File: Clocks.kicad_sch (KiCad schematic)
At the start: 87 parts, among them U1 MC100LVEL16, U13 MC100EL14, U14 1821-4731, U15 SY89421V, U16 LM311, U73 MC100LVEL16, U74 MC10EL34, U79 OSC_HS-2810

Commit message: Add component values, some more nets
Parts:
- C177, C178, C179, C182, C184, C185, C186: value ? -> 0.047uF
- C180, C202, C203, C204, C205, C206, C207, C208, C209, C210, C211, C212, C213, C214, C215: value ? -> 3.3nF
- C181: value ? -> 3.9nF
- C183, C187, C188, C189, C190: value ? -> 1nF
- C461: value ? -> 360pF
- R221, R222: value ? -> 56.2
- R223: value ? -> 38.3
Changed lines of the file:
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@@
 			)
 		)
-		(property "Value" "?"
+		(property "Value" "3.3nF"
 			(at 363.22 62.2362 0)
 			(effects
@@
 			)
 		)
-		(property "Value" "?"
+		(property "Value" "3.3nF"
 			(at 287.02 58.4262 0)
 			(effects
@@
 			)
 		)
-		(property "Value" "?"
+		(property "Value" "1nF"
 			(at 26.67 170.1862 0)
 			(effects
@@
 			)
 		)
-		(property "Value" "?"
+		(property "Value" "3.3nF"
 			(at 287.02 78.7462 0)
 			(effects
@@
 			)
 		)
-		(property "Value" "?"
+		(property "Value" "3.3nF"
 			(at 278.13 78.7462 0)
 			(effects
@@
 			)
 		)
-		(property "Value" "?"
+		(property "Value" "56.2"
 			(at 397.256 182.118 0)
 			(effects
@@
 			)
 		)
-		(property "Value" "?"
+		(property "Value" "0.047uF"
 			(at 163.83 179.0762 0)
 			(effects
@@
 			)
 		)
-		(property "Value" "?"
+		(property "Value" "1nF"
 			(at 229.108 139.192 90)
 			(effects
@@
 			)
 		)
-		(property "Value" "?"
+		(property "Value" "3.3nF"
 			(at 321.31 116.8462 0)
 			(effects
@@
 			)
 		)
-		(property "Value" "?"
+		(property "Value" "3.3nF"
 			(at 295.91 78.7462 0)
 			(effects
@@
 			)
 		)
-		(property "Value" "?"
+		(property "Value" "3.3nF"
 			(at 354.33 62.2362 0)
 			(effects
@@
 			)
 		)
-		(property "Value" "?"
+		(property "Value" "0.047uF"
 			(at 124.46 187.9662 0)
 			(effects
@@
 			)
 		)
-		(property "Value" "?"
+		(property "Value" "3.3nF"
 			(at 304.8 78.7462 0)
 			(effects
@@
 			)
 		)
-		(property "Value" "?"
+		(property "Value" "3.3nF"
 			(at 229.87 85.0962 0)
 			(effects
@@
 			)
 		)
-		(property "Value" "?"
+		(property "Value" "3.9nF"
 			(at 240.03 85.0962 0)
 			(effects
@@
 			)
 		)
-		(property "Value" "?"
+		(property "Value" "0.047uF"
 			(at 162.56 90.1762 0)
 			(effects
@@
 			)
 		)
-		(property "Value" "?"
+		(property "Value" "38.3"
 			(at 386.588 192.024 0)
 			(effects
@@
 			)
 		)
-		(property "Value" "?"
+		(property "Value" "3.3nF"
 			(at 313.69 58.4262 0)
 			(effects
@@
 			)
 		)
-		(property "Value" "?"
+		(property "Value" "3.3nF"
 			(at 313.69 78.7462 0)
 			(effects
@@
 			)
 		)
-		(property "Value" "?"
+		(property "Value" "0.047uF"
 			(at 69.342 153.416 90)
 			(effects
@@
 			)
 		)
-		(property "Value" "?"
+		(property "Value" "3.3nF"
 			(at 295.91 58.4262 0)
 			(effects
@@
 			)
 		)
-		(property "Value" "?"
+		(property "Value" "3.3nF"
 			(at 312.42 116.8462 0)
 			(effects
@@
 			)
 		)
-		(property "Value" "?"
+		(property "Value" "3.3nF"
 			(at 278.13 58.4262 0)
 			(effects
@@
 			)
 		)
-		(property "Value" "?"
+		(property "Value" "1nF"
 			(at 415.29 194.3162 0)
 			(effects
@@
 			)
 		)
-		(property "Value" "?"
+		(property "Value" "1nF"
 			(at 405.13 194.3162 0)
 			(effects
@@
 			)
 		)
-		(property "Value" "?"
+		(property "Value" "360pF"
 			(at 436.626 193.04 0)
 			(effects
@@
 			)
 		)
-		(property "Value" "?"
+		(property "Value" "3.3nF"
 			(at 304.8 58.4262 0)
 			(effects
@@
 			)
 		)
-		(property "Value" "?"
+		(property "Value" "0.047uF"
 			(at 214.63 85.0962 0)
 			(effects
@@
 			)
 		)
-		(property "Value" "?"
+		(property "Value" "56.2"
 			(at 384.048 181.864 0)
 			(effects
@@
 			)
 		)
-		(property "Value" "?"
+		(property "Value" "0.047uF"
 			(at 73.914 166.624 90)
 			(effects
@@
 			)
 		)
-		(property "Value" "?"
+		(property "Value" "1nF"
 			(at 134.62 187.9662 0)
 			(effects
@@
 			)
 		)
-		(property "Value" "?"
+		(property "Value" "0.047uF"
 			(at 104.14 90.1762 0)
 			(effects

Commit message: complete outer layers
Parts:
- RN1, RN2, RN3, RN4, RN5, RN6, RN7, RN8: footprint Resistor_SMD:R_Array_Convex_4x0603 -> hp16717:HP_R_Array_Convex_4x0603
- U13, U15: footprint Package_SO:SOIC-20W_7.5x12.8mm_P1.27mm -> hp16717:HP_SOIC-20W_7.5x12.8mm_P1.27mm
- U79: footprint Oscillator:Oscillator_DIP-14 -> hp16717:HP_Oscillator_DIP-14
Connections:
- net +3V3: no longer C211.1
- net -1V7: now also C211.1
- net 100M_SYSCLK2 renamed 100M_SYSCLK2_P
- net TZCLK1 renamed TZCLK1_P
- net TZCLK2 renamed TZCLK2_P
- net TZCLK3 renamed TZCLK3_P
- net TZCLK4 renamed TZCLK4_P
- net TZCLK5 renamed TZCLK5_P
- net TZCLKI renamed TZCLKI_P
- net TZCLKO1 renamed TZCLKO1_P
- net TZCLKO10 renamed TZCLKO10_P
- net TZCLKO2 renamed TZCLKO2_P
- net TZCLKO3 renamed TZCLKO3_P
- net TZCLKO4 renamed TZCLKO4_P
- net TZCLKO5 renamed TZCLKO5_P
- net TZCLKO6 renamed TZCLKO6_P
- net TZCLKO7 renamed TZCLKO7_P
- net TZCLKO8 renamed TZCLKO8_P
- net TZCLKO9 renamed TZCLKO9_P
- net ~{100M_SYSCLK2} renamed 100M_SYSCLK2_N
- net ~{TZCLK1} renamed TZCLK1_N
- net ~{TZCLK2} renamed TZCLK2_N
- net ~{TZCLK3} renamed TZCLK3_N
- net ~{TZCLK4} renamed TZCLK4_N
- net ~{TZCLK5} renamed TZCLK5_N
- net ~{TZCLKI} renamed TZCLKI_N
- net ~{TZCLKO10} renamed TZCLKO10_N
- net ~{TZCLKO1} renamed TZCLKO1_N
- net ~{TZCLKO2} renamed TZCLKO2_N
- net ~{TZCLKO3} renamed TZCLKO3_N
- net ~{TZCLKO4} renamed TZCLKO4_N
- net ~{TZCLKO5} renamed TZCLKO5_N
- net ~{TZCLKO6} renamed TZCLKO6_N
- net ~{TZCLKO7} renamed TZCLKO7_N
- net ~{TZCLKO8} renamed TZCLKO8_N
- net ~{TZCLKO9} renamed TZCLKO9_N
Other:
- moved on the sheet: C211

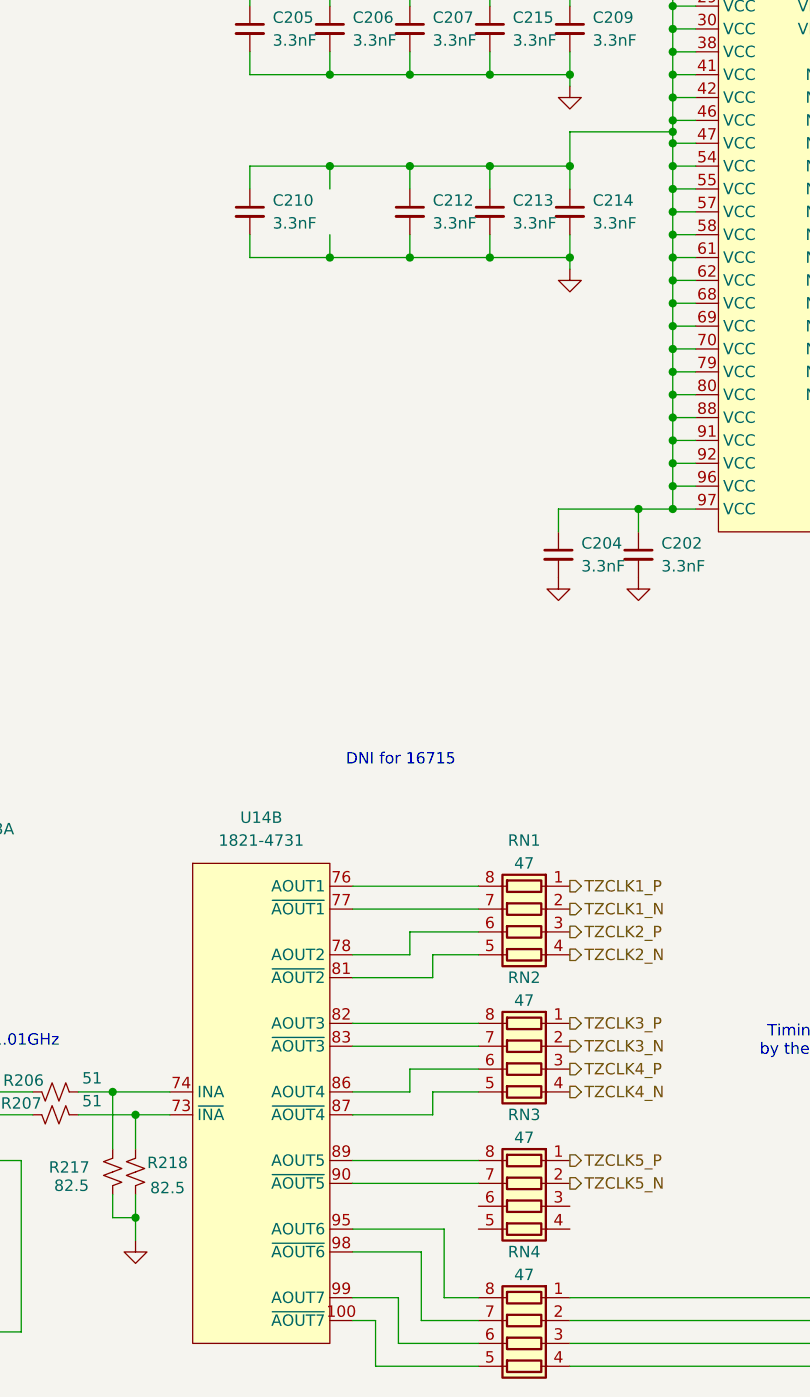
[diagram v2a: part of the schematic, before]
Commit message: schematic cleanup, arrange silk designators
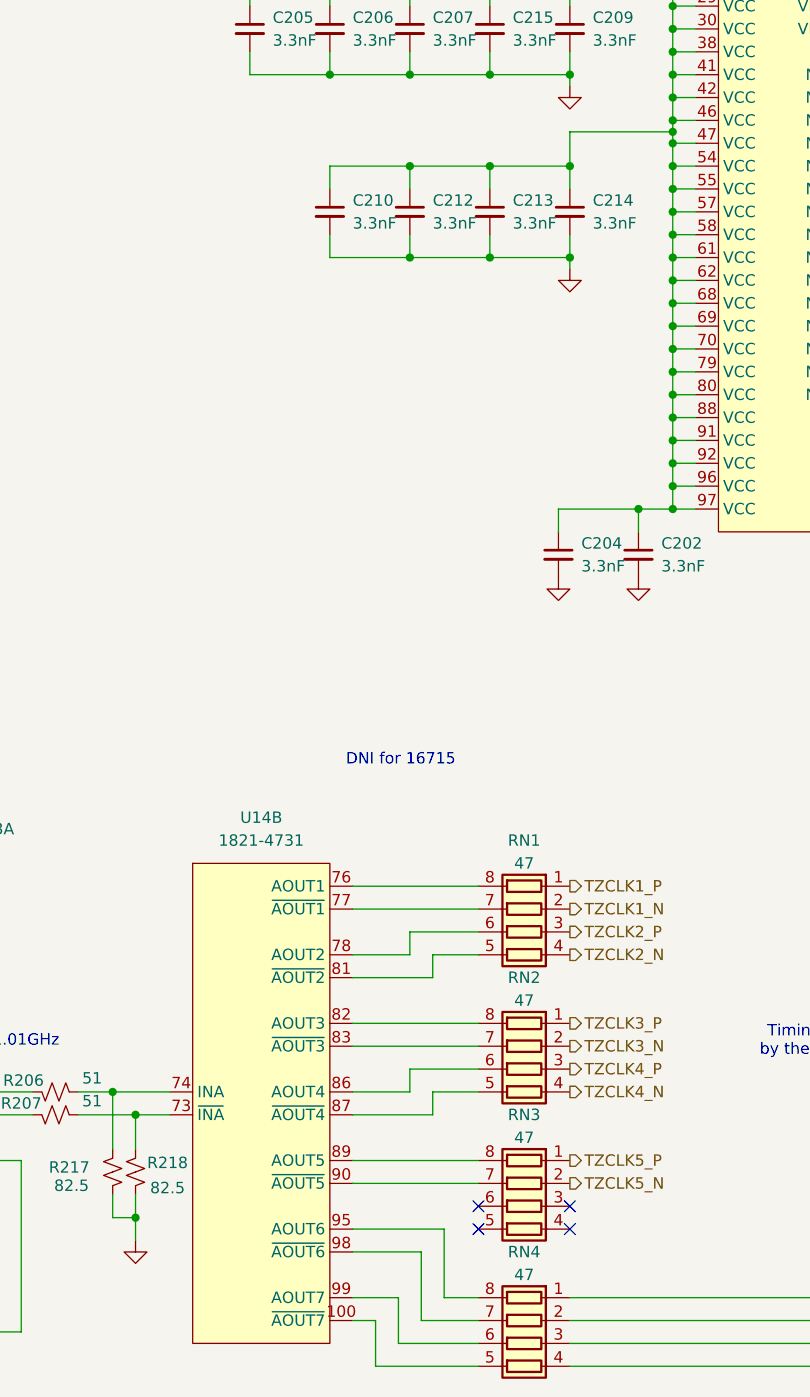
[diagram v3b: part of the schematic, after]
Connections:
- no-connect marks 10 -> 14
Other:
- moved on the sheet: C210
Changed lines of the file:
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@@
 	)
 	(junction
-		(at 284.48 72.39)
-		(diameter 0)
-		(color 0 0 0 0)
-	)
-	(junction
 		(at 311.15 72.39)
 		(diameter 0)
@@
 	)
 	(junction
-		(at 284.48 82.55)
-		(diameter 0)
-		(color 0 0 0 0)
-	)
-	(junction
 		(at 425.45 24.13)
 		(diameter 0)
@@
 	)
 	(no_connect
+		(at 311.15 190.5)
+	)
+	(no_connect
 		(at 420.37 76.2)
 	)
 	(no_connect
+		(at 300.99 187.96)
+	)
+	(no_connect
+		(at 300.99 190.5)
+	)
+	(no_connect
 		(at 435.61 177.8)
 	)
@@
 	)
 	(no_connect
+		(at 311.15 187.96)
+	)
+	(no_connect
 		(at 96.52 53.34)
 	)
@@
 	(wire
 		(pts
-			(xy 284.48 72.39) (xy 293.37 72.39)
-		)
-		(stroke
-			(width 0)
-			(type default)
-		)
-	)
-	(wire
-		(pts
 			(xy 53.34 45.72) (xy 55.88 45.72)
 		)
@@
 	(wire
 		(pts
-			(xy 284.48 82.55) (xy 284.48 80.01)
-		)
-		(stroke
-			(width 0)
-			(type default)
-		)
-	)
-	(wire
-		(pts
 			(xy 438.15 91.44) (xy 438.15 146.05)
 		)
@@
 	(wire
 		(pts
-			(xy 275.59 82.55) (xy 284.48 82.55)
+			(xy 284.48 82.55) (xy 293.37 82.55)
 		)
 		(stroke
@@
 	(wire
 		(pts
-			(xy 284.48 72.39) (xy 284.48 74.93)
-		)
-		(stroke
-			(width 0)
-			(type default)
-		)
-	)
-	(wire
-		(pts
 			(xy 420.37 57.15) (xy 443.23 57.15)
 		)
@@
 	(wire
 		(pts
-			(xy 275.59 72.39) (xy 275.59 74.93)
+			(xy 284.48 72.39) (xy 284.48 74.93)
 		)
 		(stroke
@@
 	(wire
 		(pts
-			(xy 275.59 82.55) (xy 275.59 80.01)
+			(xy 284.48 82.55) (xy 284.48 80.01)
 		)
 		(stroke
@@
 	(wire
 		(pts
-			(xy 284.48 82.55) (xy 293.37 82.55)
-		)
-		(stroke
-			(width 0)
-			(type default)
-		)
-	)
-	(wire
-		(pts
 			(xy 205.74 190.5) (xy 205.74 185.42)
 		)
@@
 	(wire
 		(pts
-			(xy 275.59 72.39) (xy 284.48 72.39)
+			(xy 284.48 72.39) (xy 293.37 72.39)
 		)
 		(stroke
@@
 	(symbol
 		(lib_id "Device:C_Small")
-		(at 275.59 77.47 0)
+		(at 284.48 77.47 0)
 		(unit 1)
 		(exclude_from_sim no)
@@
 		(dnp no)
 		(property "Reference" "C210"
-			(at 278.13 76.2062 0)
+			(at 287.02 76.2062 0)
 			(effects
 				(font
@@
 		)
 		(property "Value" "3.3nF"
-			(at 278.13 78.7462 0)
+			(at 287.02 78.7462 0)
 			(effects
 				(font
@@
 		)
 		(property "Footprint" "hp16717:HP_0603"
-			(at 275.59 77.47 0)
+			(at 284.48 77.47 0)
 			(effects
 				(font
@@
 		)
 		(property "Datasheet" "~"
-			(at 275.59 77.47 0)
+			(at 284.48 77.47 0)
 			(effects
 				(font
@@
 		)
 		(property "Description" "Unpolarized capacitor, small symbol"
-			(at 275.59 77.47 0)
+			(at 284.48 77.47 0)
 			(effects
 				(font

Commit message: add test points
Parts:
- added TP1069, TP1070, TP1072, TP1073, TP670, TP671, TP672, TP673, TP674, TP675, TP676, TP808, TP809, TP810, TP811, TP812, TP813, TP816, TP817, TP818, TP823, TP824: ?, hp16717:HP_TP30, symbol Connector:TestPoint_Alt
- added TP1071: +3V3, hp16717:HP_TP30, symbol Connector:TestPoint_Alt
- added TP661, TP807: HPCLK_D0, hp16717:HP_TP30, symbol Connector:TestPoint_Alt
- added TP662, TP806: HPCLK_D1, hp16717:HP_TP30, symbol Connector:TestPoint_Alt
- added TP663, TP804: HPCLK_D3, hp16717:HP_TP30, symbol Connector:TestPoint_Alt
- added TP664, TP805: HPCLK_D2, hp16717:HP_TP30, symbol Connector:TestPoint_Alt
- added TP665, TP800: HPCLK_D7, hp16717:HP_TP30, symbol Connector:TestPoint_Alt
- added TP666, TP801: HPCLK_D6, hp16717:HP_TP30, symbol Connector:TestPoint_Alt
- added TP667, TP802: HPCLK_D5, hp16717:HP_TP30, symbol Connector:TestPoint_Alt
- added TP668, TP803: HPCLK_D4, hp16717:HP_TP30, symbol Connector:TestPoint_Alt
- added TP669, TP677: 3V3, hp16717:HP_TP30, symbol Connector:TestPoint_Alt
- added TP814: +5V, hp16717:HP_TP30, symbol Connector:TestPoint_Alt
- added TP815, TP825, TP826: GND, hp16717:HP_TP30, symbol Connector:TestPoint_Alt
- added TP819: VBB, hp16717:HP_TP30, symbol Connector:TestPoint_Alt
- added TP820: FOUT, hp16717:HP_TP30, symbol Connector:TestPoint_Alt
- added TP821: ~{FOUT}, hp16717:HP_TP30, symbol Connector:TestPoint_Alt
- added TP822, TP829: +3V3A, hp16717:HP_TP30, symbol Connector:TestPoint_Alt
- added TP827: VFILT, hp16717:HP_TP30, symbol Connector:TestPoint_Alt
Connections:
- net +3V3: now also TP1071.1, TP669.1, TP677.1
- net +3V3A: now also TP822.1, TP829.1
- net +5V: now also TP814.1
- net GND: now also TP1072.1, TP1073.1, TP815.1, TP825.1, TP826.1
- net HPCLK_D0: now also TP807.1
- net HPCLK_D1: now also TP806.1
- net HPCLK_D2: now also TP805.1
- net HPCLK_D3: now also TP804.1
- net HPCLK_D4: now also TP803.1
- net HPCLK_D5: now also TP802.1
- net HPCLK_D6: now also TP801.1
- net HPCLK_D7: now also TP800.1
- net VFILT: now also TP827.1
- net at R208.1, U15.15 (FOUT), U15.2 (FIN): now also TP820.1
- net at C185.1, R199.2, R501.2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: now also TP816.1
- net at C182.1, R199.1, R200.1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: now also TP819.1
- net at RP1.16 (R1.2), RP14.1 (R1.1), U14.5 (UNK): now also TP670.1
- net at RP1.15 (R2.2), RP14.2 (R2.1), U14.4 (UNK): now also TP671.1
- net at RP1.14 (R3.2), RP14.3 (R3.1), U14.22 (UNK): now also TP672.1
- net at RP1.13 (R4.2), RP14.4 (R4.1), U14.21 (UNK): now also TP673.1
- net at RP1.12 (R5.2), RP14.5 (R5.1), U14.20 (UNK): now also TP674.1
- net at RP1.11 (R6.2), RP14.6 (R6.1), U14.94 (UNK): now also TP675.1
- net at RP1.10 (R7.2), RP14.7 (R7.1), U14.6 (UNK): now also TP676.1
- net at R184.2, U13.15 (CLK), U74.5 (~{Q1}): now also TP812.1
- net at R185.2, U13.14 (~{CLK}), U74.4 (Q1): now also TP811.1
- net at R186.2, U13.16 (SCLK), U74.1 (Q0): now also TP809.1
- net at R216.2, R220.2, U14.3 (~{INB}): now also TP1070.1
- net at C186.1, R200.2, R525.2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: now also TP817.1
- net at R201.2, U15.18 (~{RIN}), U73.6 (~{Q}): now also TP824.1
- net at R202.2, U15.19 (RIN), U73.7 (Q): now also TP823.1
- net at RP15.7 (R7.1), RP2.10 (R7.2), U14.10 (UNK): now also TP662.1
- net at RP15.6 (R6.1), RP2.11 (R6.2), U14.11 (UNK): now also TP664.1
- net at RP15.5 (R5.1), RP2.12 (R5.2), U14.12 (UNK): now also TP663.1
- net at RP15.4 (R4.1), RP2.13 (R4.2), U14.14 (UNK): now also TP668.1
- net at RP15.3 (R3.1), RP2.14 (R3.2), U14.15 (UNK): now also TP667.1
- net at RP15.2 (R2.1), RP2.15 (R2.2), U14.16 (UNK): now also TP666.1
- net at RP15.1 (R1.1), RP2.16 (R1.2), U14.17 (UNK): now also TP665.1
- net at RP15.8 (R8.1), RP2.9 (R8.2), U14.9 (UNK): now also TP661.1
- net at R224.2, U14.93 (UNK), U16.2 (+): now also TP818.1
- net at R183.2, U74.2 (~{Q0}): now also TP810.1
- net at C179.1, R187.2, R188.2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: now also TP808.1
- net at R205.1, U15.14 (~{FOUT}), U15.3 (~{FIN}): now also TP821.1
- net at R215.2, R219.2, U14.2 (INB): now also TP1069.1
- net at R226.2, R227.1, U16.3 (-): now also TP813.1
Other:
- moved on the sheet: RP1, RP14

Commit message: tweaks and some schematic notes
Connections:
- net at RN4.5 (R4.2): now also U14.100 (~{BOUT10}); no longer U14.100 (~{AOUT7})
- net at RN4.6 (R3.2): now also U14.99 (BOUT10); no longer U14.99 (AOUT7)
- net at RN4.7 (R2.2): now also U14.98 (~{BOUT9}); no longer U14.98 (~{AOUT6})
- net at RN4.8 (R1.2): now also U14.95 (BOUT9); no longer U14.95 (AOUT6)
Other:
- note added: "0.9V/1.3V"
- note added: "1.3V/1.7V"
- note added: "2.5VH/1.7VL"
- note added: "HIGH=DIV BY 4, LOW=DIV BY 1?"
- note added: "HIGH?"
- note added: "LOW WHEN CLOCK OUT ACTIVE"
- note added: "LOW?"
- note added: "PULSES HIGH BEFORE CLOCK BURST OUT"
- note added: "THIS SECTION CAN DIVIDE CLOCK INPUT"
- note added: "THIS SECTION JUST SEEMS TO BE A FANOUT BUFFER"
- note added: "TRIGGER?"
- moved on the sheet: R226, R227, RN4, TP813, TP818
